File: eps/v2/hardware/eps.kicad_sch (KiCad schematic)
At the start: 0 parts

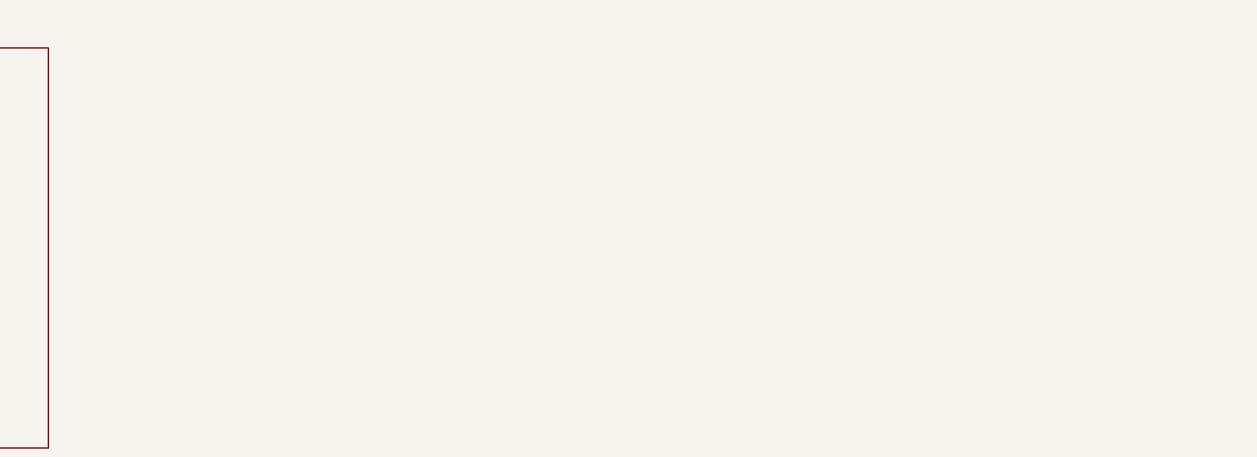
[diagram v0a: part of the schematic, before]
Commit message: Add Pack & USB-C mux (#173) and I2C mux eFuse control (#178) subsheets
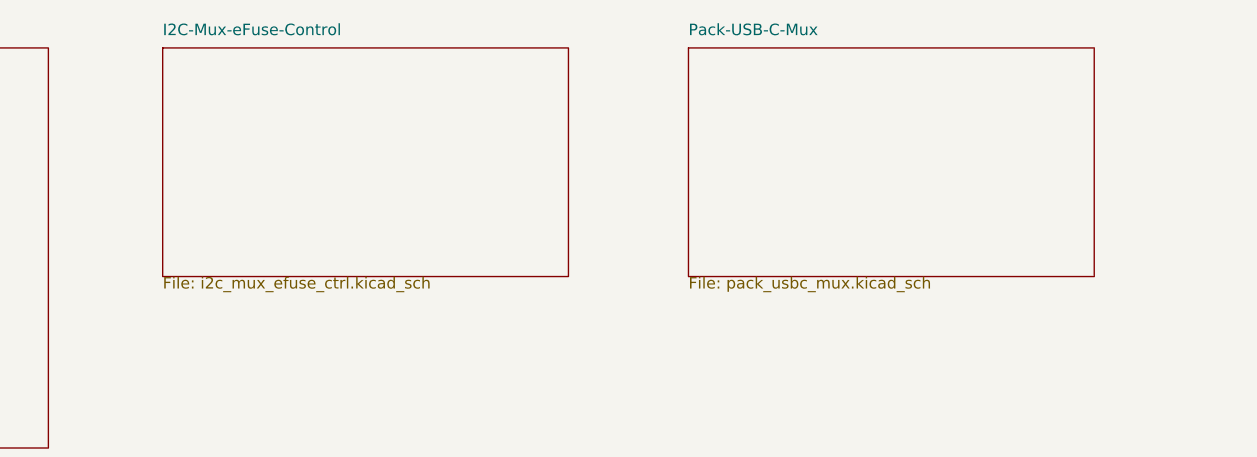
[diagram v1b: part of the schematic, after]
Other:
- added sheet I2C-Mux-eFuse-Control (i2c_mux_efuse_ctrl.kicad_sch)
- added sheet Pack-USB-C-Mux (pack_usbc_mux.kicad_sch)
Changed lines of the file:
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@@
+		)
+	)
+	(sheet
+		(at 76.2 20.32)
+		(size 45.085 25.4)
+		(exclude_from_sim no)
+		(in_bom yes)
+		(on_board yes)
+		(dnp no)
+		(fields_autoplaced yes)
+		(stroke
+			(width 0.1524)
+			(type solid)
+		)
+		(fill
+			(color 0 0 0 0)
+		)
+		(property "Sheetname" "I2C-Mux-eFuse-Control"
+			(at 76.2 19.05 0)
+			(show_name no)
+			(do_not_autoplace no)
+			(effects
+				(font
+					(size 1.27 1.27)
+				)
+				(justify left bottom)
+			)
+		)
+		(property "Sheetfile" "i2c_mux_efuse_ctrl.kicad_sch"
+			(at 76.2 45.72 0)
+			(show_name no)
+			(do_not_autoplace no)
+			(effects
+				(font
+					(size 1.27 1.27)
+				)
+				(justify left top)
+			)
+		)
+		(instances
+			(project "eps"
+				(path "/b20f5a9e-495e-48d8-8648-bd5c7d9b4620"
+					(page "3")
+				)
+			)
+		)
+	)
+	(sheet
+		(at 134.62 20.32)
+		(size 45.085 25.4)
+		(exclude_from_sim no)
+		(in_bom yes)
+		(on_board yes)
+		(dnp no)
+		(fields_autoplaced yes)
+		(stroke
+			(width 0.1524)
+			(type solid)
+		)
+		(fill
+			(color 0 0 0 0)
+		)
+		(property "Sheetname" "Pack-USB-C-Mux"
+			(at 134.62 19.05 0)
+			(show_name no)
+			(do_not_autoplace no)
+			(effects
+				(font
+					(size 1.27 1.27)
+				)
+				(justify left bottom)
+			)
+		)
+		(property "Sheetfile" "pack_usbc_mux.kicad_sch"
+			(at 134.62 45.72 0)
+			(show_name no)
+			(do_not_autoplace no)
+			(effects
+				(font
+					(size 1.27 1.27)
+				)
+				(justify left top)
+			)
+		)
+		(instances
+			(project "eps"
+				(path "/b20f5a9e-495e-48d8-8648-bd5c7d9b4620"
+					(page "4")
+				)
+			)
 		)
 	)

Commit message: wip fuel gauge
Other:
- added sheet Fuel-Gage (Fuel_gage.kicad_sch)
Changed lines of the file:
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@@
-	)
-	(sheet
-		(at 18.415 20.32)
-		(size 45.085 44.45)
-		(exclude_from_sim no)
-		(in_bom yes)
-		(on_board yes)
-		(dnp no)
-		(fields_autoplaced yes)
-		(stroke
-			(width 0.1524)
-			(type solid)
-		)
-		(fill
-			(color 0 0 0 0)
-		)
-		(property "Sheetname" "Inter-Board-Connector"
-			(at 18.415 19.6084 0)
-			(show_name no)
-			(do_not_autoplace no)
-			(effects
-				(font
-					(size 1.27 1.27)
-				)
-				(justify left bottom)
-			)
-		)
-		(property "Sheetfile" "inter_board_connector.kicad_sch"
-			(at 18.415 65.3546 0)
-			(show_name no)
-			(do_not_autoplace no)
-			(effects
-				(font
-					(size 1.27 1.27)
-				)
-				(justify left top)
-			)
-		)
-		(instances
-			(project "eps"
-				(path "/b20f5a9e-495e-48d8-8648-bd5c7d9b4620"
-					(page "2")
-				)
-			)
-		)
 	)
 	(sheet
@@
 				)
 			)
+		)
+	)
+	(sheet
+		(at 189.23 20.32)
+		(size 26.67 15.24)
+		(exclude_from_sim no)
+		(in_bom yes)
+		(on_board yes)
+		(dnp no)
+		(fields_autoplaced yes)
+		(stroke
+			(width 0.1524)
+			(type solid)
+		)
+		(fill
+			(color 0 0 0 0)
+		)
+		(property "Sheetname" "Fuel-Gage"
+			(at 189.23 19.6084 0)
+			(show_name no)
+			(do_not_autoplace no)
+			(effects
+				(font
+					(size 1.27 1.27)
+				)
+				(justify left bottom)
+			)
+		)
+		(property "Sheetfile" "Fuel_gage.kicad_sch"
+			(at 189.23 36.1446 0)
+			(show_name no)
+			(do_not_autoplace no)
+			(effects
+				(font
+					(size 1.27 1.27)
+				)
+				(justify left top)
+			)
+		)
+		(instances
+			(project "eps"
+				(path "/b20f5a9e-495e-48d8-8648-bd5c7d9b4620"
+					(page "5")
+				)
+			)
+		)
+	)
+	(sheet
+		(at 18.415 20.32)
+		(size 45.085 44.45)
+		(exclude_from_sim no)
+		(in_bom yes)
+		(on_board yes)
+		(dnp no)
+		(fields_autoplaced yes)
+		(stroke
+			(width 0.1524)
+			(type solid)
+		)
+		(fill
+			(color 0 0 0 0)
+		)
+		(property "Sheetname" "Inter-Board-Connector"
+			(at 18.415 19.6084 0)
+			(show_name no)
+			(do_not_autoplace no)
+			(effects
+				(font
+					(size 1.27 1.27)
+				)
+				(justify left bottom)
+			)
+		)
+		(property "Sheetfile" "inter_board_connector.kicad_sch"
+			(at 18.415 65.3546 0)
+			(show_name no)
+			(do_not_autoplace no)
+			(effects
+				(font
+					(size 1.27 1.27)
+				)
+				(justify left top)
+			)
+		)
+		(instances
+			(project "eps"
+				(path "/b20f5a9e-495e-48d8-8648-bd5c7d9b4620"
+					(page "2")
+				)
+			)
